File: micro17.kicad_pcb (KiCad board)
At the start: 4 copper layers, 20 x 30 mm, 92 parts, among them J1 Conn_01x05, J2 AXK640347YG, J4 USB_B_Micro, U1 STM32G473CCUx, U2 XC6220B331MR, U3 CPC1117N, U4 MCP6002, U5 MCP4451-503-ST, U6 MCP6002, U7 MCP6002, Y1 8 MHz

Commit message: initial commit, not complete.
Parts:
- removed J2: AXK640347YG, micro17:AXK640347YG
- added C36: 100n, Capacitor_SMD:C_0603_1608Metric_Pad1.08x0.95mm_HandSolder, F.Cu at (87.5, 93.3)
- added C37: 100n, Capacitor_SMD:C_0603_1608Metric_Pad1.08x0.95mm_HandSolder, F.Cu at (83.8, 93.3)
- added H1: MountingHole_Pad, MountingHole:MountingHole_2.7mm_M2.5_DIN965_Pad_TopBottom, F.Cu at (53.0, 53.0)
- added H2: MountingHole_Pad, MountingHole:MountingHole_2.7mm_M2.5_DIN965_Pad_TopBottom, F.Cu at (87.0, 53.0)
- added H3: MountingHole_Pad, MountingHole:MountingHole_2.7mm_M2.5_DIN965_Pad_TopBottom, F.Cu at (87.0, 97.0)
- added H4: MountingHole_Pad, MountingHole:MountingHole_2.7mm_M2.5_DIN965_Pad_TopBottom, F.Cu at (53.0, 97.0)
- added J3: Conn_01x09, Connector_PinHeader_2.54mm:PinHeader_1x09_P2.54mm_Vertical, F.Cu at (59.9, 97.0)
- added J6: Conn_01x40_Pin, Connector_FFC-FPC:Hirose_FH12-40S-0.5SH_1x40-1MP_P0.50mm_Horizontal, F.Cu at (68.2, 88.0)
- added JP1: Jumper_3_Open, Jumper:SolderJumper-3_P1.3mm_Open_RoundedPad1.0x1.5mm_NumberLabels, F.Cu at (74.0, 82.8)
- added R30: 22k, Resistor_SMD:R_0603_1608Metric_Pad0.98x0.95mm_HandSolder, F.Cu at (17.8, 86.5)
- added R31: 12k, Resistor_SMD:R_0603_1608Metric_Pad0.98x0.95mm_HandSolder, F.Cu at (17.8, 83.0)
- added U11: TXS0108EPW, Package_SO:TSSOP-20_4.4x6.5mm_P0.65mm, F.Cu at (85.8, 89.0)
- added U8: TXS0102DCU, Package_SO:VSSOP-8_2.3x2mm_P0.5mm, F.Cu at (32.2, 96.6)
- C1, C11, C12, C13, C14, C15, C16, C17, C18, C19, C2, C20, C21, C22, C23, C24, C25, C29, C3, C30, C31, C32, C33, C35, C4, C5, C6, C7, C8, C9: footprint Capacitor_SMD:C_0402_1005Metric -> Capacitor_SMD:C_0603_1608Metric_Pad1.08x0.95mm_HandSolder
- C10: footprint Capacitor_SMD:C_0805_2012Metric -> Capacitor_SMD:C_0805_2012Metric_Pad1.18x1.45mm_HandSolder
- D1, TP10, TP11, TP13, TP3, TP4, TP5, TP6, TP7, TP8, TP9, U3: moved to F.Cu
- FB1: footprint Inductor_SMD:L_0603_1608Metric_Pad1.05x0.95mm_HandSolder -> Inductor_SMD:L_0805_2012Metric_Pad1.15x1.40mm_HandSolder
- J4: footprint Connector_USB:USB_Micro-B_Molex_47346-0001 -> Connector_USB:USB_Micro-B_Amphenol_10103594-0001LF_Horizontal; moved to F.Cu
- R1, R10, R11, R12, R13, R14, R15, R16, R17, R18, R19, R2, R20, R21, R22, R23, R26, R27, R28, R29, R3, R4, R5, R6, R7, R8, R9: footprint Resistor_SMD:R_0402_1005Metric -> Resistor_SMD:R_0603_1608Metric_Pad0.98x0.95mm_HandSolder
- R24: footprint Resistor_SMD:R_0603_1608Metric -> Resistor_SMD:R_0603_1608Metric_Pad0.98x0.95mm_HandSolder
- R25: footprint Resistor_SMD:R_0402_1005Metric -> Resistor_SMD:R_0603_1608Metric_Pad0.98x0.95mm_HandSolder; moved to F.Cu
- moved TP8 175.5 mm to (24.5, 89.8), turned to 0 degrees
- moved TP6 173.3 mm to (21.5, 89.8), turned to 0 degrees
- moved TP13 165.5 mm to (32.6, 89.8)
- moved TP5 163.8 mm to (21.5, 86.8), turned to 0 degrees
- moved TP7 163.2 mm to (24.5, 86.8), turned to 0 degrees
- moved TP11 158.8 mm to (32.6, 86.8), turned to 0 degrees
- moved TP10 156.0 mm to (27.6, 89.8), turned to 0 degrees
- moved TP9 154.0 mm to (27.6, 86.8), turned to 0 degrees
- moved J4 141.9 mm to (52.8, 60.8), turned to -90 degrees
- moved C10 137.8 mm to (45.4, 70.1)
- moved U2 137.7 mm to (45.4, 65.2)
- moved C13 137.6 mm to (45.3, 68.2)
- moved FB1 137.6 mm to (45.4, 72.5)
- moved C11 137.3 mm to (45.3, 62.3)
- moved C28 130.2 mm to (65.0, 80.2), turned to 90 degrees
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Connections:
- C8 pad 1: /MCU/VDDA -> VDDA
- C9 pad 2: /MCU/VDDA -> VDDA
- R1 pad 2: +3V3 -> VDDA
- R26 pad 1: +3V3 -> VDDA
- R29 pad 2: Net-(U1-PC13) -> PTT_IN
- R4 pad 1: PTT_IN -> PTT_IN_5V
- R4 pad 2: Net-(U1-PC13) -> PTT_IN
- R5 pad 1: /MCU/VDDA -> VDDA
- U1 pad 2: Net-(U1-PC13) -> PTT_IN
- U1 pad 21: /MCU/VDDA -> VDDA
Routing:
- net +3V3: track 69.1 -> 33.7 mm, vias 8 -> 6
- net GND: track 35.6 -> 1.76 mm, vias 61 -> 1
- net BUS+_5V: track 0.00 -> 25.5 mm
- net CH_Activity_5V: track 0.00 -> 24.8 mm
- net GP4_IN_OUT_ACC8_5V: track 0.00 -> 24.3 mm, vias 0 -> 2
- net GP1_IN_ACC3_5V: track 0.00 -> 23.9 mm
- net Net-(U5B-P1A): track 27.7 -> 4.69 mm
- net EXP_BD_REQ_5V: track 0.00 -> 21.9 mm, vias 0 -> 2
- net Net-(U5A-P0A): track 20.4 -> 2.28 mm, vias 3 -> 1
- net PTT_IN_5V: track 0.00 -> 17.9 mm
- net PTT_OUT: track 16.6 -> 0.00 mm, vias 1 -> 0
- net AUDIO_OUT_MUTE: track 16.2 -> 0.00 mm, vias 2 -> 0
- net VDDA: track 0.00 -> 16.1 mm
- net I2C_SCL: track 23.5 -> 7.52 mm, vias 2 -> 1
- net PTT_IN: track 18.9 -> 3.16 mm, vias 1 -> 2
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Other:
- board size 20 x 30 mm -> 40 x 50 mm
- board text added: "RF-022"
- board text added: "RF60 https://www.altinkaya.com.tr/urunler/rf-kutular"
- board text removed: "Aout"

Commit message: .
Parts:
- removed TP10, TP13, TP6, TP8, TP9: GP, TestPoint:TestPoint_Pad_D1.0mm
- added Q1: BC817, Package_TO_SOT_SMD:SOT-23, F.Cu at (82.2, 97.0)
- added R32: 3k3, Resistor_SMD:R_0603_1608Metric_Pad0.98x0.95mm_HandSolder, F.Cu at (78.8, 94.4)
- J1, U8: moved to B.Cu
- moved TP5 66.2 mm to (80.8, 57.4)
- moved TP7 64.2 mm to (88.6, 83.6)
- moved TP11 45.2 mm to (63.6, 53.9)
- moved U8 41.2 mm to (73.3, 93.9), turned to 0 degrees
- moved R31 36.6 mm to (53.4, 91.2), turned to -90 degrees
- moved R30 34.4 mm to (51.8, 91.2)
- moved J1 19.8 mm to (70.6, 52.6)
- moved J3 1.45 mm to (58.4, 97.0)
- moved R29 0.40 mm to (70.6, 79.0)
- moved C12 0.27 mm to (66.9, 64.6)
- moved C23 0.27 mm to (63.8, 64.6)
- moved C5 0.27 mm to (77.8, 64.6)
- moved C7 0.27 mm to (76.3, 64.6)
- moved C8 0.27 mm to (71.7, 64.6)
- moved C9 0.27 mm to (73.2, 64.6)
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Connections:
- J3 pad 1: Net-(J3-Pin_1) -> GND
- J3 pad 2: +5VD -> BASEBAND_IN
- J3 pad 3: Net-(J3-Pin_3) -> AUDIO_OUT_FILT
- J3 pad 4: BASEBAND_OUT_FILT -> AUDIO_IN
- J3 pad 5: AUDIO_IN -> BASEBAND_OUT_FILT
- J3 pad 6: AUDIO_OUT_FILT -> Net-(J3-Pin_6)
- J3 pad 7: BASEBAND_IN -> +5VD
- J3 pad 8: GND -> Net-(J3-Pin_8)
- J3 pad 9: unconnected-(J3-Pin_9-Pad9) -> Net-(J3-Pin_9)
- TP5 pad 1: +5VD -> MCU_RX
- U8 pad 1: Net-(J3-Pin_3) -> Net-(J3-Pin_6)
- U8 pad 8: Net-(J3-Pin_1) -> Net-(J3-Pin_8)
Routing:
- net AUDIO_OUT_FILT: track 0.00 -> 51.7 mm, vias 0 -> 2
- net Net-(U5A-P0A): track 2.28 -> 31.7 mm, vias 1 -> 3
- net +3V3: track 33.7 -> 62.3 mm, vias 6 -> 8
- net Net-(U5B-P1A): track 4.69 -> 32.0 mm
- net I2C_SCL: track 7.52 -> 32.9 mm, vias 1 -> 2
- net BASEBAND_OUT_FILT: track 6.21 -> 27.3 mm, vias 0 -> 1
- net AUDIO_OUT: track 0.00 -> 19.9 mm, vias 0 -> 2
- net PTT_OUT: track 0.00 -> 19.2 mm, vias 0 -> 2
- net AUDIO_IN: track 5.73 -> 23.6 mm, vias 0 -> 1
- net I2C_SDA: track 7.29 -> 24.4 mm
- net VERSION_SET: track 2.51 -> 18.5 mm, vias 1 -> 2
- net MCU_RX: track 4.93 -> 20.9 mm
- net BASEBAND_IN: track 5.01 -> 19.4 mm, vias 0 -> 1
- net EXP1_CS_5V: track 0.00 -> 14.2 mm, vias 0 -> 2
- net +5V: track 64.8 -> 78.7 mm
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
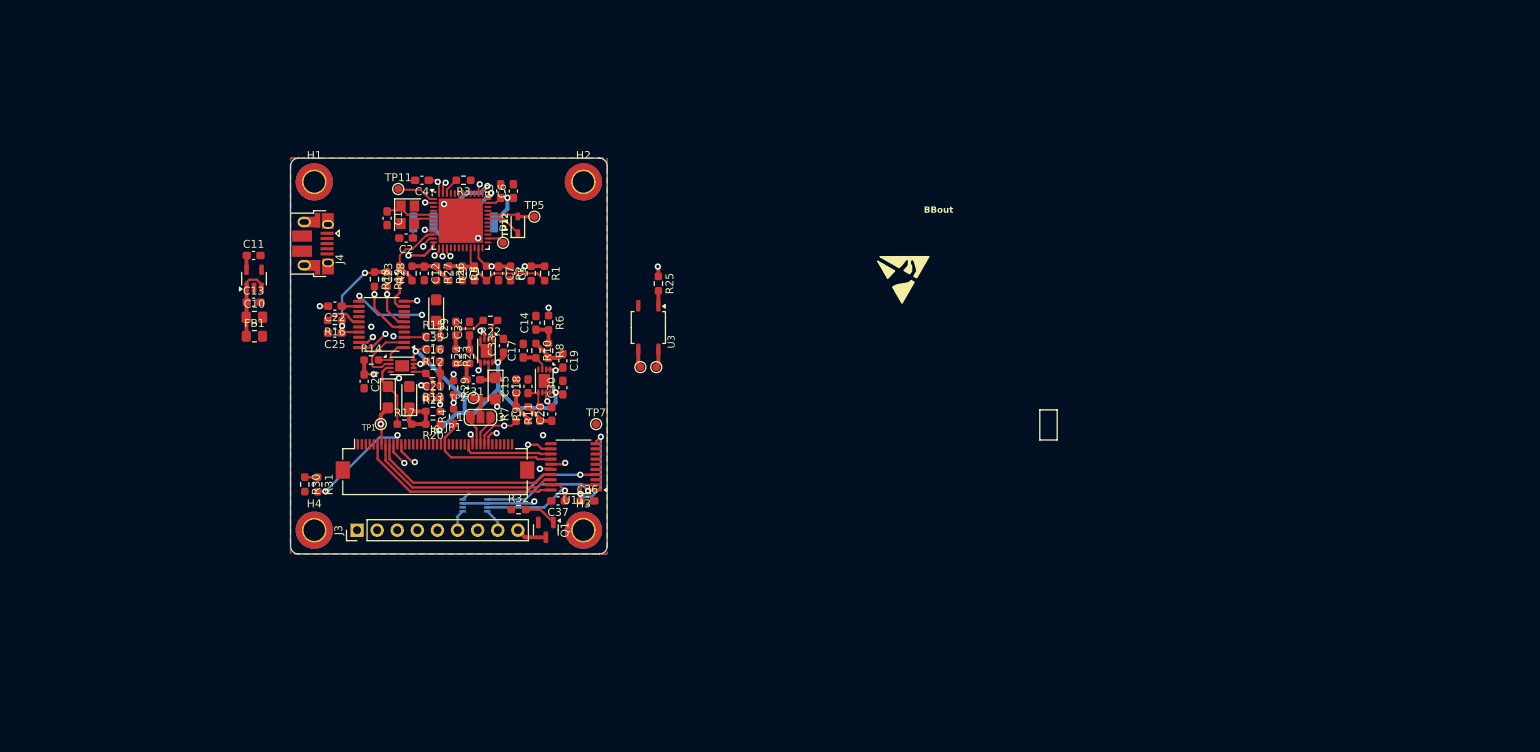
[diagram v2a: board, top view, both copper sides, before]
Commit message: PCB shape is created. Most of routing done.
Todo: assign pins for radio control signals.
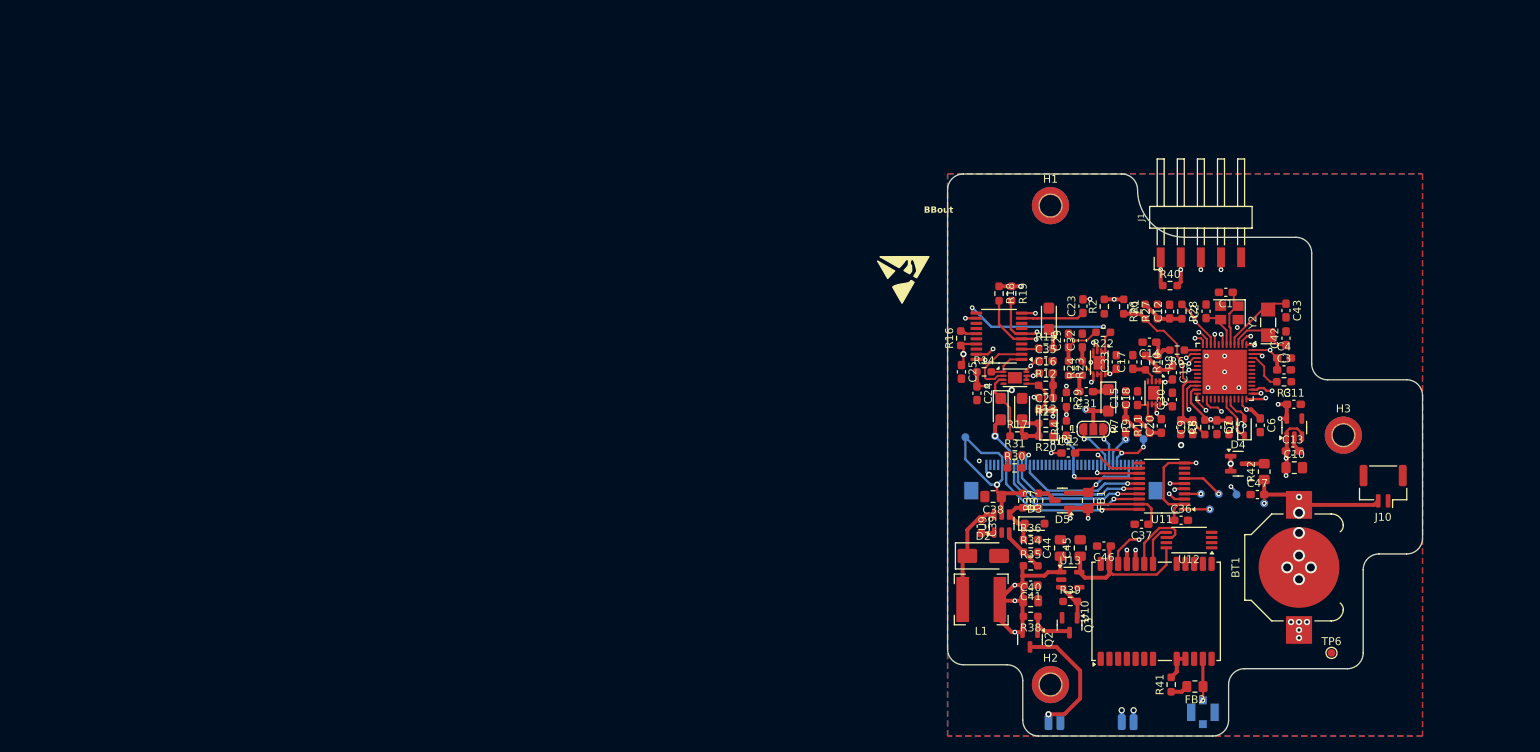
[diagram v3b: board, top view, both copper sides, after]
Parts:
- removed H4: MountingHole_Pad, MountingHole:MountingHole_2.7mm_M2.5_DIN965_Pad_TopBottom
- removed J3: Conn_01x09, Connector_PinHeader_2.54mm:PinHeader_1x09_P2.54mm_Vertical
- removed J4: USB_B_Micro, Connector_USB:USB_Micro-B_Amphenol_10103594-0001LF_Horizontal
- removed Q1: BC817, Package_TO_SOT_SMD:SOT-23
- removed R25, R32: 3k3, Resistor_SMD:R_0603_1608Metric_Pad0.98x0.95mm_HandSolder
- removed TP3, TP4: GP, TestPoint:TestPoint_Pad_D1.0mm
- removed U3: CPC1117N, Package_SO:SOP-4_3.8x4.1mm_P2.54mm
- removed U8: TXS0102DCU, Package_SO:VSSOP-8_2.3x2mm_P0.5mm
- added BT1: Battery_Cell, Battery:BatteryHolder_Keystone_3000_1x12mm, F.Cu at (177.4, 101.7)
- added C38: 22u/25V, Capacitor_SMD:C_0805_2012Metric_Pad1.18x1.45mm_HandSolder, F.Cu at (138.8, 92.8)
- added C39: 150n, Capacitor_SMD:C_0603_1608Metric_Pad1.08x0.95mm_HandSolder, F.Cu at (137.2, 96.5)
- added C40: 47u, Capacitor_SMD:C_0805_2012Metric, F.Cu at (143.5, 105.9)
- added C41: 100n, Capacitor_SMD:C_0603_1608Metric_Pad1.08x0.95mm_HandSolder, F.Cu at (143.5, 103.9)
- added C42: 4p7, Capacitor_SMD:C_0603_1608Metric_Pad1.08x0.95mm_HandSolder, F.Cu at (175.8, 72.8)
- added C43: 4p7, Capacitor_SMD:C_0603_1608Metric_Pad1.08x0.95mm_HandSolder, F.Cu at (175.8, 69.2)
- added C44: 22u/25V, Capacitor_SMD:C_0805_2012Metric_Pad1.18x1.45mm_HandSolder, F.Cu at (147.2, 99.2)
- added C45: 22u/25V, Capacitor_SMD:C_0805_2012Metric_Pad1.18x1.45mm_HandSolder, F.Cu at (149.8, 99.2)
- added C46: 100n, Capacitor_SMD:C_0603_1608Metric_Pad1.08x0.95mm_HandSolder, F.Cu at (152.8, 99.0)
- added C47: 1u, Capacitor_SMD:C_0603_1608Metric_Pad1.08x0.95mm_HandSolder, F.Cu at (172.1, 92.5)
- added D2: MS110, Diode_SMD:D_SMA, F.Cu at (137.5, 100.2)
- added D3: 3V9, Diode_SMD:D_SOD-323_HandSoldering, F.Cu at (144.0, 96.2)
- added D4: BAT54C, Package_TO_SOT_SMD:SOT-23, F.Cu at (169.7, 88.6)
- added D5: BAT54C, Package_TO_SOT_SMD:SOT-23, F.Cu at (147.5, 93.2)
- added FB2: FerriteBead_Small, Inductor_SMD:L_0805_2012Metric_Pad1.15x1.40mm_HandSolder, F.Cu at (164.2, 116.8)
- added J10: Conn_01x02_Pin, Connector_JST:JST_GH_SM02B-GHS-TB_1x02-1MP_P1.25mm_Horizontal, F.Cu at (188.0, 91.5)
- added J2: Conn_01x40_Pin, Connector_FFC-FPC:Hirose_FH12-40S-0.5SH_1x40-1MP_P0.50mm_Horizontal, B.Cu at (147.7, 90.6)
- added J5: Conn_01x01_Pin, Connector_Wire:SolderWirePad_1x01_SMD_1x2mm, B.Cu at (156.5, 121.2)
- added J7: Conn_01x01_Pin, Connector_Wire:SolderWirePad_1x01_SMD_1x2mm, B.Cu at (145.8, 121.2)
- added J8: Conn_01x01_Pin, Connector_Wire:SolderWirePad_1x01_SMD_1x2mm, B.Cu at (147.2, 121.2)
- added J9: Conn_Coaxial, Connector_Coaxial:U.FL_Molex_MCRF_73412-0110_Vertical, B.Cu at (165.2, 120.0)
- added L1: 15u, Inductor_SMD:L_Bourns-SRN6028, F.Cu at (137.2, 105.8)
- added Q2: DMP3056, Package_TO_SOT_SMD:SOT-23, F.Cu at (143.4, 110.8)
- added Q3: 2N7002, Package_TO_SOT_SMD:SOT-23, F.Cu at (148.4, 109.0)
- added R33: 3k3, Resistor_SMD:R_0603_1608Metric_Pad0.98x0.95mm_HandSolder, F.Cu at (144.5, 93.2)
- added R34: 10k, Resistor_SMD:R_0603_1608Metric_Pad0.98x0.95mm_HandSolder, F.Cu at (143.5, 99.8)
- added R35: 56k, Resistor_SMD:R_0603_1608Metric_Pad0.98x0.95mm_HandSolder, F.Cu at (143.5, 101.5)
- added R36: 10k, Resistor_SMD:R_0603_1608Metric_Pad0.98x0.95mm_HandSolder, F.Cu at (143.5, 98.2)
- added R37: 36k, Resistor_SMD:R_0603_1608Metric_Pad0.98x0.95mm_HandSolder, F.Cu at (142.5, 93.2)
- added R38: 10k, Resistor_SMD:R_0603_1608Metric_Pad0.98x0.95mm_HandSolder, F.Cu at (143.5, 107.9)
- added R39: 10k, Resistor_SMD:R_0603_1608Metric_Pad0.98x0.95mm_HandSolder, F.Cu at (148.5, 106.0)
- added R40: 3k3, Resistor_SMD:R_0603_1608Metric_Pad0.98x0.95mm_HandSolder, F.Cu at (161.1, 66.1)
- added R41: 10R, Resistor_SMD:R_0603_1608Metric_Pad0.98x0.95mm_HandSolder, F.Cu at (161.2, 116.5)
- added R42: 100R, Resistor_SMD:R_0805_2012Metric_Pad1.20x1.40mm_HandSolder, F.Cu at (173.0, 89.6)
- added TP10: GP, TestPoint:TestPoint_Pad_D1.0mm, B.Cu at (165.0, 92.4)
- added TP13: GP, TestPoint:TestPoint_Pad_D1.0mm, B.Cu at (135.2, 85.2)
- added TP6: GP, TestPoint:TestPoint_Pad_D1.0mm, F.Cu at (181.5, 112.5)
- added TP8: GP, TestPoint:TestPoint_Pad_D1.0mm, B.Cu at (157.8, 85.5)
- added TP9: GP, TestPoint:TestPoint_Pad_D1.0mm, B.Cu at (155.5, 85.5)
- added U10: NEO-6M, RF_GPS:ublox_NEO, F.Cu at (159.3, 107.2)
- added U12: AT24CS32-XHM, Package_SO:TSSOP-8_4.4x3mm_P0.65mm, F.Cu at (163.5, 98.2)
- added U13: XC6220B331MR, Package_TO_SOT_SMD:SOT-23-5, F.Cu at (148.5, 103.2)
- added U9: LMR14206, Package_TO_SOT_SMD:SOT-23-6, F.Cu at (139.8, 96.2)
- added Y2: ECS-.327-12.5-34QCS-TR, Crystal:Crystal_SMD_EuroQuartz_EQ161-2Pin_3.2x1.5mm_HandSoldering, F.Cu at (173.5, 70.8)
- J1: moved to F.Cu
- J6: value Conn_01x40_Pin -> Conn_01x01_Pin; footprint Connector_FFC-FPC:Hirose_FH12-40S-0.5SH_1x40-1MP_P0.50mm_Horizontal -> Connector_Wire:SolderWirePad_1x01_SMD_1x2mm; moved to B.Cu
- TP1, TP11, TP12, TP2, TP5, TP7: moved to B.Cu
- moved C11 132.8 mm to (176.8, 81.1)
- moved U2 132.8 mm to (176.8, 84.0)
- moved C10 132.7 mm to (176.8, 89.1)
- moved C13 132.6 mm to (176.6, 87.0)
- moved TP11 116.4 mm to (173.0, 93.6), turned to 180 degrees
- moved C4 111.2 mm to (175.5, 75.2), turned to 0 degrees
- moved FB1 107.3 mm to (150.8, 93.2), turned to -90 degrees
- moved R3 106.7 mm to (175.5, 78.2)
- moved C1 106.4 mm to (168.2, 67.0), turned to 180 degrees
- moved Y1 104.5 mm to (168.6, 69.5), turned to 180 degrees
- moved C3 101.5 mm to (175.5, 76.8), turned to 0 degrees
- moved C2 101.5 mm to (165.7, 69.3), turned to 90 degrees
- moved C6 98.9 mm to (172.5, 83.8), turned to -90 degrees
- moved U1 98.4 mm to (168.0, 77.0), turned to -90 degrees
- moved TP12 98.0 mm to (169.5, 92.5), turned to 180 degrees
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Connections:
- net Net-(U1-VBAT) renamed +BATT
- FB1 pad 1: +5V -> +5VD
- FB1 pad 2: +5VD -> +5V
- J6 pad 1: GND -> USART3_RX
- U1 pad 22: unconnected-(U1-PB10-Pad22) -> USART3_TX
- U1 pad 24: unconnected-(U1-PB11-Pad24) -> USART3_RX
- U1 pad 3: unconnected-(U1-PC14-Pad3) -> /MCU/PC14
- U1 pad 4: unconnected-(U1-PC15-Pad4) -> /MCU/PC15
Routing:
- net +BATT: track 4.98 -> 82.3 mm, vias 0 -> 10
- net +5V: track 78.7 -> 148.9 mm, vias 5 -> 11
- net USART3_TX: track 0.00 -> 54.4 mm, vias 0 -> 3
- net PTT_IN: track 2.86 -> 55.6 mm, vias 2 -> 3
- net USART3_RX: track 0.00 -> 48.1 mm, vias 0 -> 3
- net AUDIO_OUT_FILT: track 51.7 -> 12.0 mm
- net 13V2: track 0.00 -> 24.5 mm, vias 0 -> 1
- net Net-(U5A-P0W): track 2.19 -> 25.1 mm, vias 0 -> 2
- net BASEBAND_OUT_FILT: track 27.3 -> 6.56 mm
- net GPS_POWER: track 0.00 -> 20.0 mm
- net AUDIO_IN: track 23.6 -> 4.80 mm
- net AUDIO_OUT: track 19.9 -> 1.65 mm, vias 2 -> 0
- net Net-(J7-Pin_1): track 0.00 -> 16.9 mm, vias 0 -> 1
- net /MCU/~{RST}: track 0.00 -> 15.4 mm, vias 0 -> 2
- net BASEBAND_OUT: track 19.3 -> 34.5 mm
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- added copper zone on In1.Cu, net +3V3
- removed copper zone on In1.Cu, net GND
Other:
- board size 40 x 50 mm -> 60 x 71 mm
- board text added: "Front"
- board text added: "Middle"
- board text added: "Side"
- board text removed: "RF-022"
- board text removed: "RF60 https://www.altinkaya.com.tr/urunler/rf-kutular"

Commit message: end of day commit
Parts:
- added C48: 100n, Capacitor_SMD:C_0603_1608Metric_Pad1.08x0.95mm_HandSolder, F.Cu at (164.5, 66.1)
- added C49: 100p, Capacitor_SMD:C_0603_1608Metric_Pad1.08x0.95mm_HandSolder, F.Cu at (153.2, 117.9)
- added C50: 100p, Capacitor_SMD:C_0603_1608Metric_Pad1.08x0.95mm_HandSolder, F.Cu at (158.1, 117.9)
- added C51: 100n, Capacitor_SMD:C_0603_1608Metric_Pad1.08x0.95mm_HandSolder, F.Cu at (151.0, 117.9)
- added J11: Ext_Tamper, Jumper:SolderJumper-2_P1.3mm_Open_RoundedPad1.0x1.5mm, F.Cu at (157.2, 65.6)
- added R43: 3k3, Resistor_SMD:R_0603_1608Metric_Pad0.98x0.95mm_HandSolder, F.Cu at (154.8, 117.9)
- added R44: 3k3, Resistor_SMD:R_0603_1608Metric_Pad0.98x0.95mm_HandSolder, F.Cu at (156.5, 117.9)
- added SW1: SW_Push, Button_Switch_SMD:SW_SPST_TL3305B, F.Cu at (160.1, 69.4)
- moved R28 13.3 mm to (149.3, 68.7)
- moved C12 10.2 mm to (150.9, 68.7)
- moved TP12 9.17 mm to (165.2, 84.4)
- moved R27 8.21 mm to (152.5, 65.1)
- moved R26 5.49 mm to (152.5, 68.7)
- moved R2 4.03 mm to (154.5, 65.1), turned to -90 degrees
- moved C23 2.40 mm to (147.7, 68.7)
- moved J5 1.50 mm to (155.0, 121.2)
- moved J6 1.50 mm to (156.5, 121.2)
- moved C46 1.03 mm to (153.4, 98.2), turned to 90 degrees
- moved C5 0.81 mm to (167.8, 84.4)
- moved C7 0.81 mm to (166.3, 84.4)
- moved C8 0.81 mm to (161.8, 84.4)
- moved C9 0.81 mm to (163.3, 84.4)
- moved R5 0.81 mm to (164.8, 84.4)
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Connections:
- J5 pad 1: USART3_TX -> Net-(J5-Pin_1)
- J6 pad 1: USART3_RX -> Net-(J6-Pin_1)
- U1 pad 17: unconnected-(U1-PB0-Pad17) -> POWER_CONTROL
- U1 pad 19: unconnected-(U1-PB2-Pad19) -> GPS_EN
- U1 pad 28: unconnected-(U1-PB15-Pad28) -> OPT_CS
- U1 pad 41: unconnected-(U1-PB3-Pad41) -> CH_Activity
- U1 pad 8: unconnected-(U1-PA0-Pad8) -> TAMPER
- U11 pad 8: RDY -> AUDIO_OUT_MUTE
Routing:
- net GPS_EN: track 4.88 -> 42.7 mm, vias 0 -> 2
- net POWER_CONTROL: track 9.68 -> 41.9 mm, vias 0 -> 2
- net CH_Activity: track 2.20 -> 25.1 mm, vias 1 -> 2
- net AUDIO_OUT_MUTE: track 1.06 -> 22.2 mm, vias 1 -> 2
- net TAMPER: track 0.00 -> 12.8 mm
- net OPT_CS: track 0.00 -> 12.1 mm, vias 0 -> 2
- net Net-(U1-PB13): track 14.2 -> 4.48 mm, vias 2 -> 1
- net Net-(J11-Pin_2): track 0.00 -> 9.52 mm
- net USART3_TX: track 54.4 -> 46.4 mm
- net USART3_RX: track 48.1 -> 44.5 mm
- net PTT_IN: track 55.6 -> 59.0 mm
- net Net-(J5-Pin_1): track 0.00 -> 2.52 mm, vias 0 -> 1
- net Net-(J6-Pin_1): track 0.00 -> 2.49 mm, vias 0 -> 1
- net Net-(U5B-P1W): track 8.62 -> 6.22 mm
- net unconnected-(U1-PA8-Pad30): track 0.00 -> 2.08 mm, vias 0 -> 1
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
